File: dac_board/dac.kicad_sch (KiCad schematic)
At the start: 15 parts, among them IC1 ES9039Q2M, IC2 ES9312Q

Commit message: More updates, finished DAC block
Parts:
- removed C28: 1u, symbol Device:C_Small
- removed R15, R19: 47k, symbol Device:R
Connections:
- net GNDD: now also IC1.20 (MISO/ADDR0/MUTE_CTRL), IC1.21 (GPIO1), IC1.22 (GPIO2), IC1.23 (GPIO3), IC1.29 (MODE); no longer IC1.15 (SCLK/SCL/HW1), IC1.16 (MOSI/SDA/HW0)
- net I2S_BCLK: now reaches IC1.12 (DATA_CLK)
- net I2S_WS: now reaches IC1.13 (DATA1)
- net I2S_DATA: now reaches IC1.14 (DATA2)
- new net I2C_SCL: IC1.15 (SCLK/SCL/HW1)
- new net I2C_SDA: IC1.16 (MOSI/SDA/HW0)
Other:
- note added: "ENABLE_64FS_MODE = 1 r DAC_MODE = 1 r PCM_MASTER_MODE=1 r MASTER_BCK_DIV=0 # Use with 49.152 MHz clock to have 768 kHz i2s w/ 32-bit channels (64FS)r SYNC_MODE = ? # Device should pull data only if needed by default; set SYNC_MODE to SYNC if having trouble"
- note added: "There is no HW mode for a 768 kHz i2s master, but this can be achieved through software configuration (i2c). Non-Default (Sub)Register Values:"
- title: (none) -> DAC and DAC Power

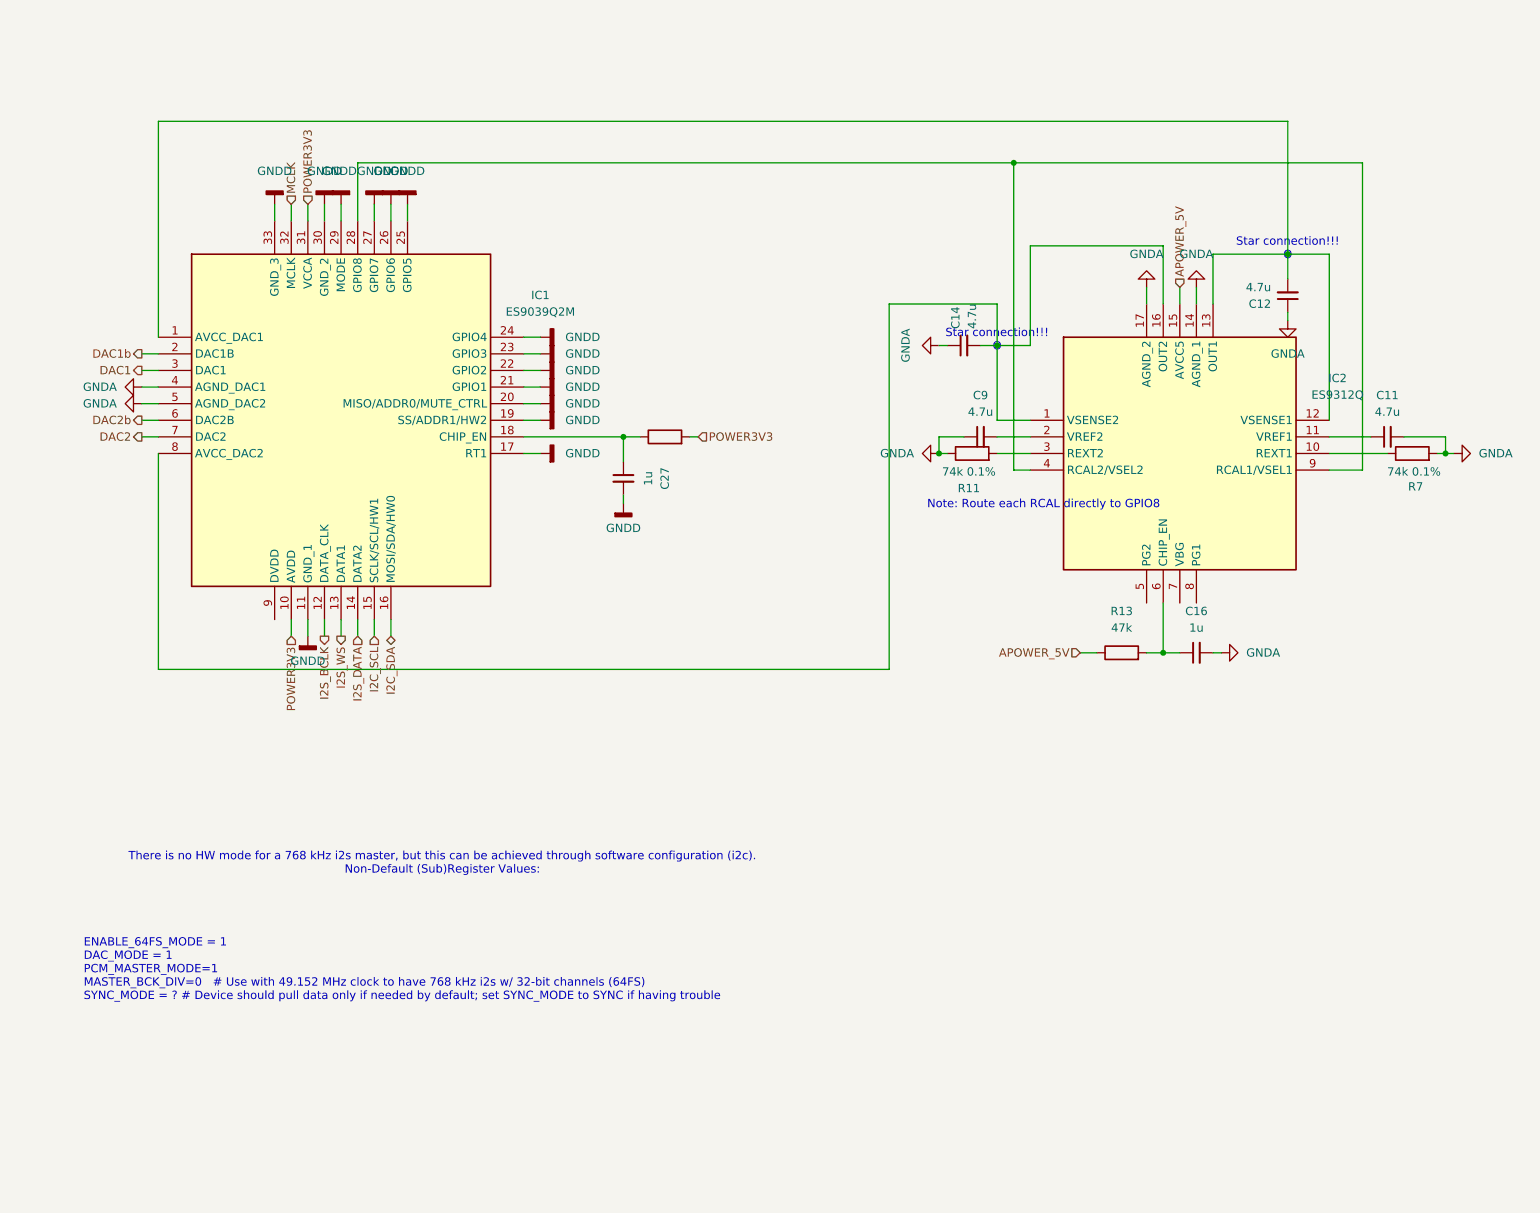
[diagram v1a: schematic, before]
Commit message: Added MCU and associated logic
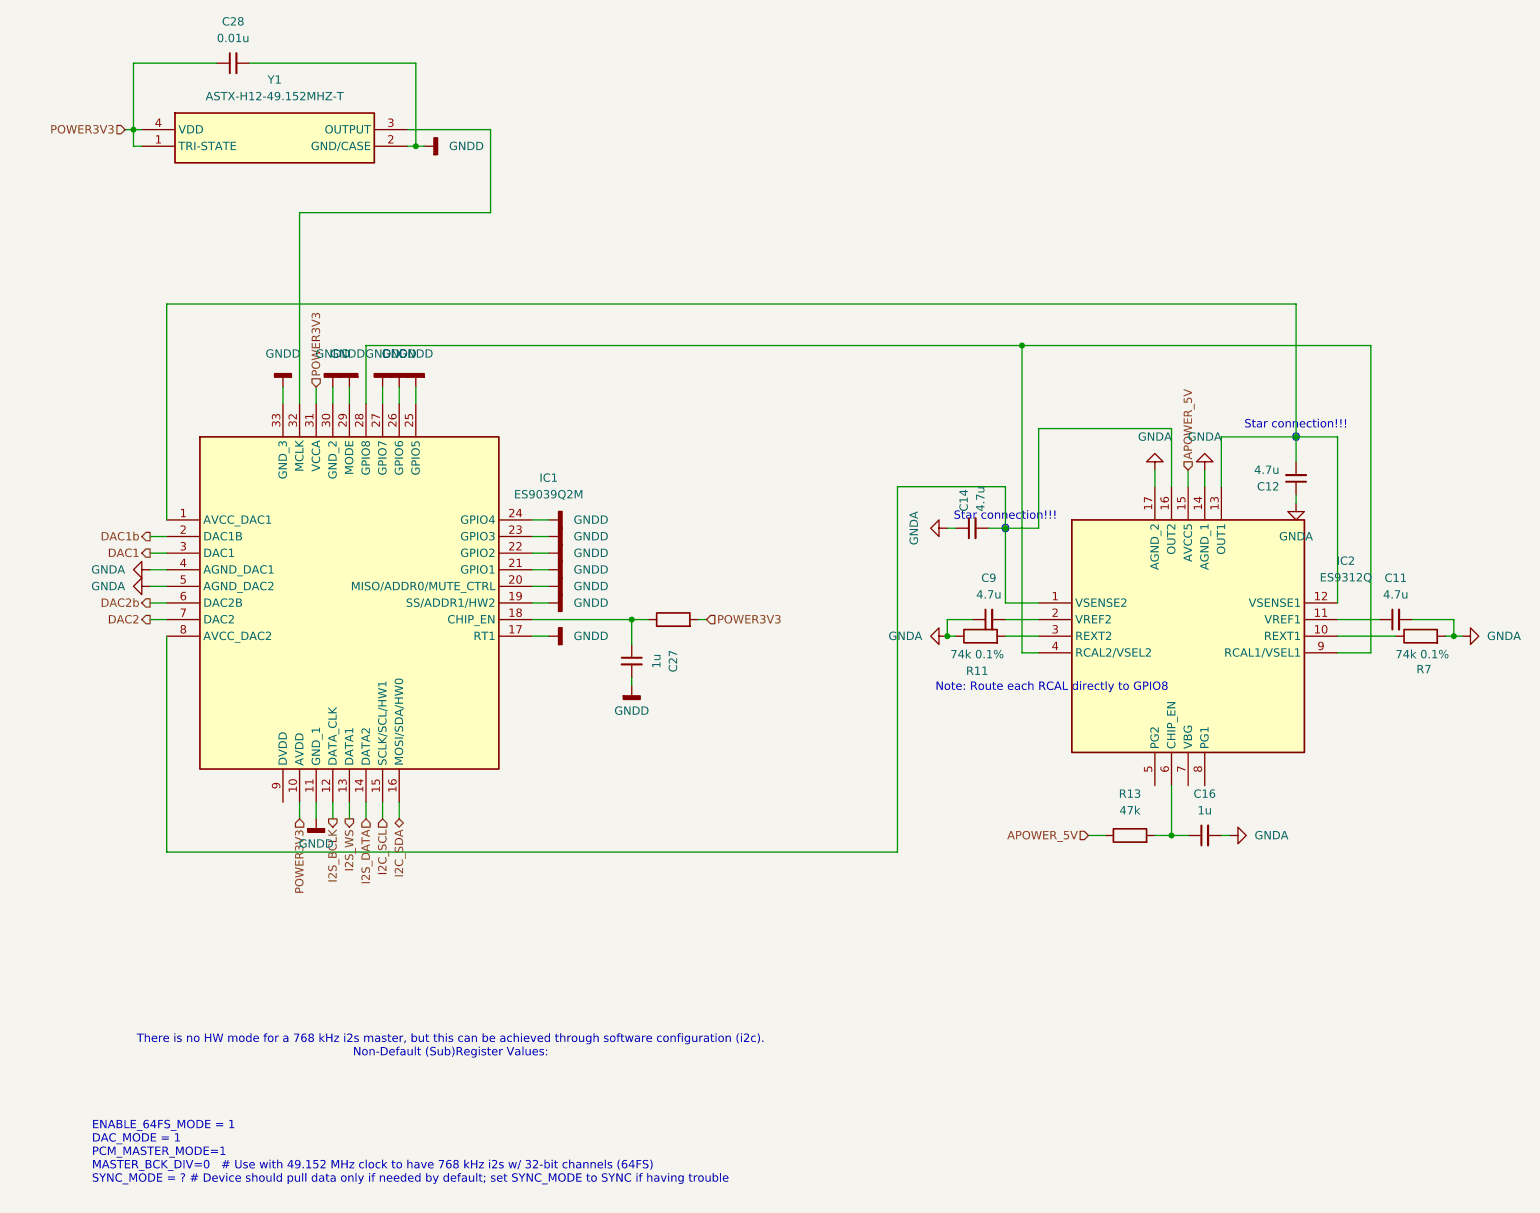
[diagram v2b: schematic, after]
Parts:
- added C28: 0.01u, symbol Device:C_Small
- added Y1: ASTX-H12-49.152MHZ-T, ASTX-H12, symbol ASTX-H12-49_152MHZ-T:ASTX-H12-49.152MHZ-T
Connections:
- net GNDD: now also C28.2, Y1.2 (GND/CASE)
- net POWER3V3: now also C28.1, Y1.1 (TRI-STATE), Y1.4 (VDD)
- net MCLK: no longer names the net of IC1.32 (MCLK)
- net MCLK: now also Y1.3 (OUTPUT)
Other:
- moved on the sheet: C11, C12, C14, C16, C27, C9, IC1, IC2, R11, R13, R7

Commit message: Finished schematic design for MCU + DAC
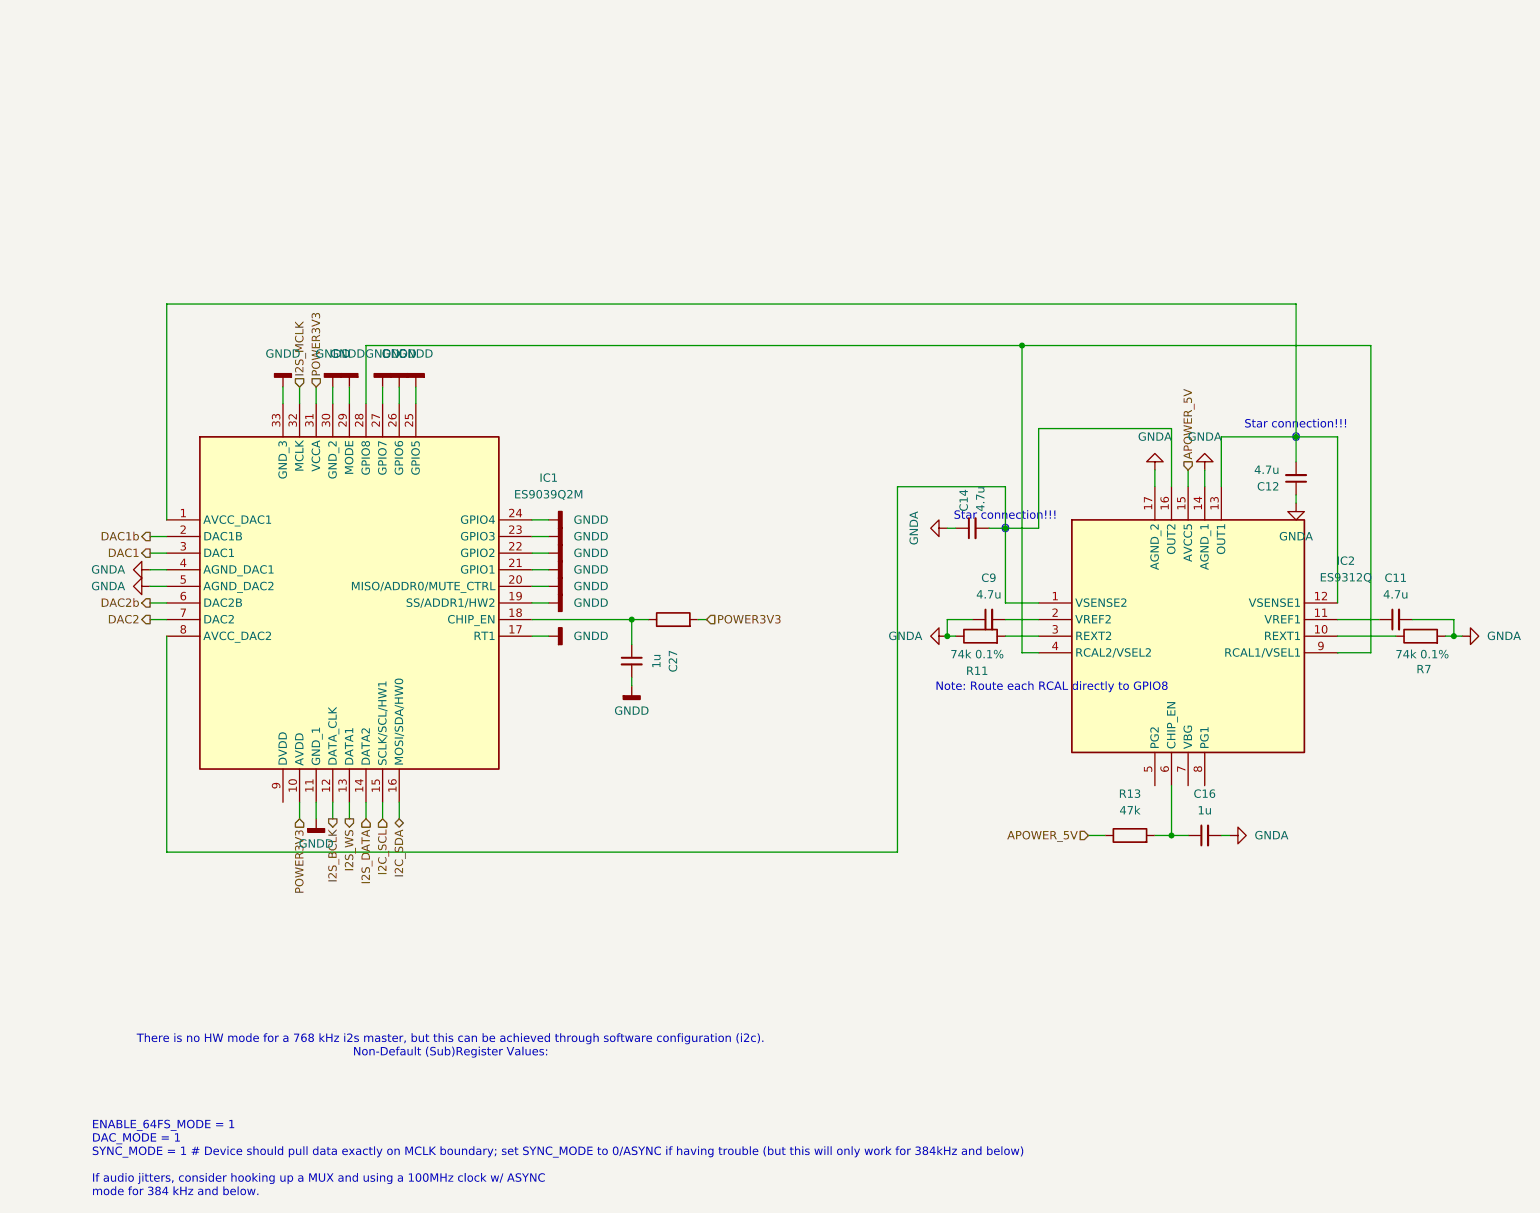
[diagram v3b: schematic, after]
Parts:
- removed C28: 0.01u, symbol Device:C_Small
- removed Y1: ASTX-H12-49.152MHZ-T, ASTX-H12, symbol ASTX-H12-49_152MHZ-T:ASTX-H12-49.152MHZ-T
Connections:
- net I2S_MCLK: now reaches IC1.32 (MCLK)
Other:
- note added: "ENABLE_64FS_MODE = 1r DAC_MODE = 1r SYNC_MODE = 1 # Device should pull data exactly on MCLK boundary; set SYNC_MODE to 0/ASYNC if having trouble (but this will only work for 384kHz and below) If audio jitters, consider hooking up a MUX and using a 100MHz clock w/ ASYNC mode for 384 kHz and below."
- note removed: "ENABLE_64FS_MODE = 1 r DAC_MODE = 1 r PCM_MASTER_MODE=1 r MASTER_BCK_DIV=0 # Use with 49.152 MHz clock to have 768 kHz i2s w/ 32-bit channels (64FS)r SYNC_MODE = ? # Device should pull data only if needed by default; set SYNC_MODE to SYNC if having trouble"

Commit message: Added TVS protection, USB CC handling, grounded MCU pins, impedance-matched HF traces, and increased output current capability per consultation with circuit-board-design.com
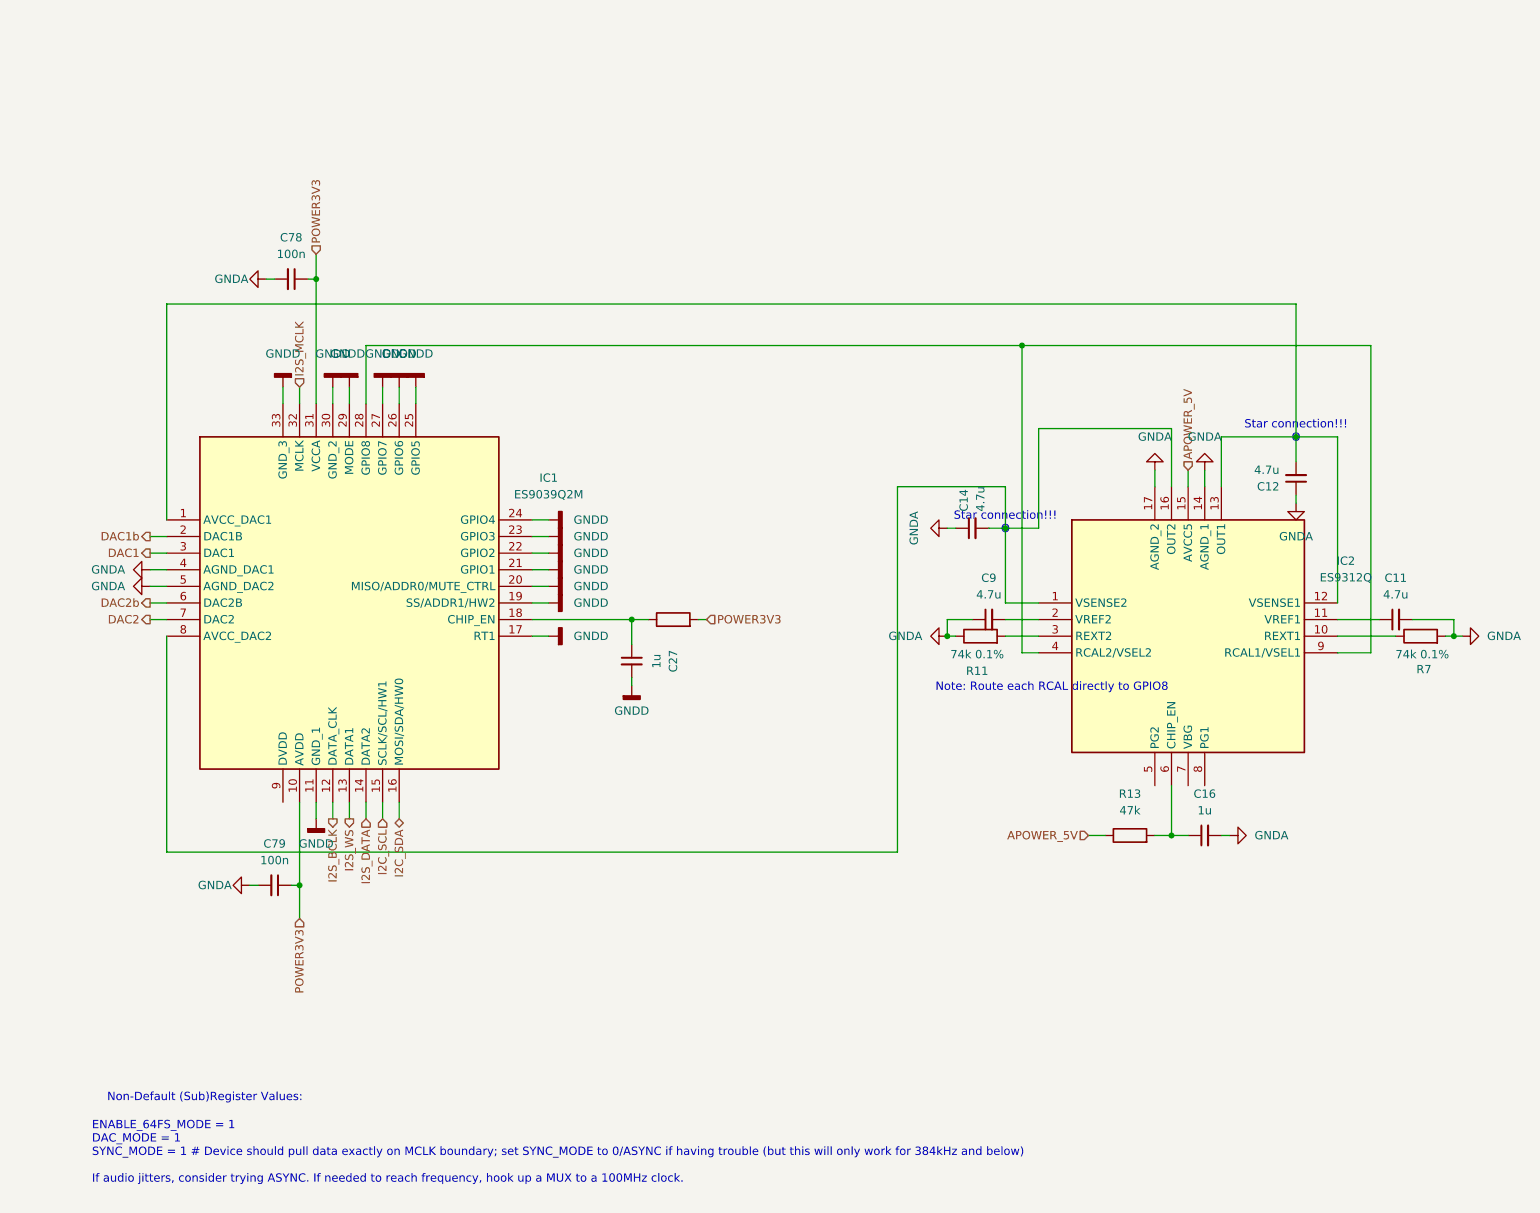
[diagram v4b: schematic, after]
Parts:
- added C78, C79: 100n, symbol Device:C_Small
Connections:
- net GNDA: now also C78.2, C79.2
- net POWER3V3: now also C78.1, C79.1
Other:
- note added: "ENABLE_64FS_MODE = 1r DAC_MODE = 1r SYNC_MODE = 1 # Device should pull data exactly on MCLK boundary; set SYNC_MODE to 0/ASYNC if having trouble (but this will only work for 384kHz and below) If audio jitters, consider trying ASYNC. If needed to reach frequency, hook up a MUX to a 100MHz clock."
- note added: "Non-Default (Sub)Register Values:"
- note removed: "ENABLE_64FS_MODE = 1r DAC_MODE = 1r SYNC_MODE = 1 # Device should pull data exactly on MCLK boundary; set SYNC_MODE to 0/ASYNC if having trouble (but this will only work for 384kHz and below) If audio jitters, consider hooking up a MUX and using a 100MHz clock w/ ASYNC mode for 384 kHz and below."
- note removed: "There is no HW mode for a 768 kHz i2s master, but this can be achieved through software configuration (i2c). Non-Default (Sub)Register Values:"
